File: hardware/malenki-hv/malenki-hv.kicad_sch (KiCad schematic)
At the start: 18 parts, among them J1 Conn_01x02_Male-Connector, J2 Conn_01x08_Male, J3 Conn_01x02, U2 AP2204RA-3.3TRG1, U3 ATTiny1616-MNR

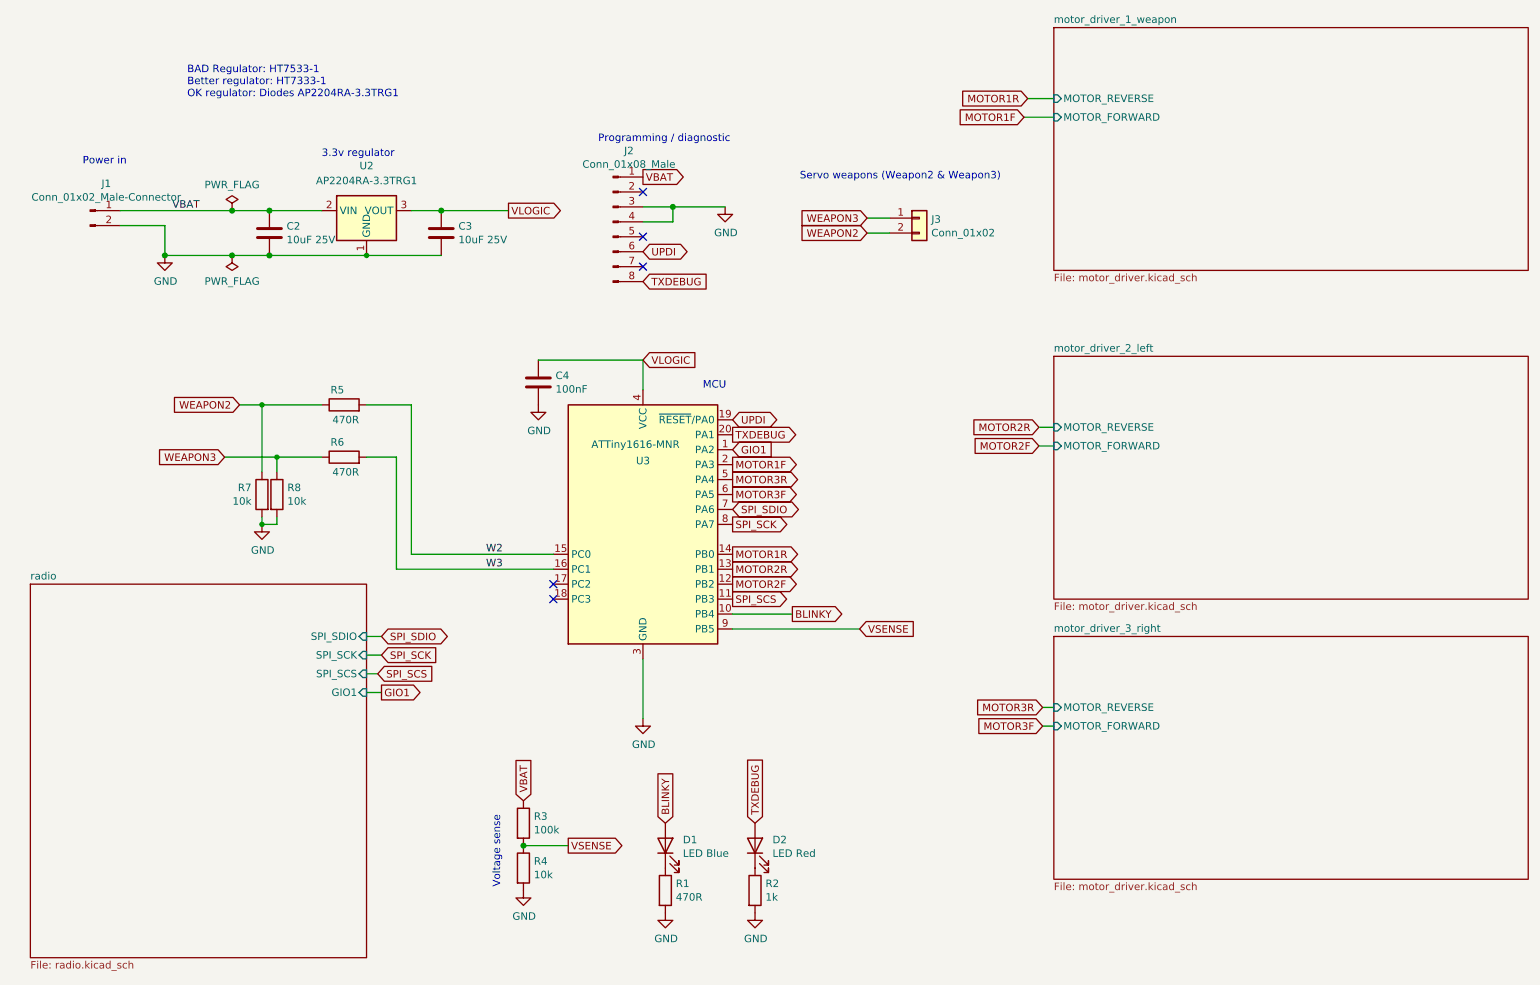
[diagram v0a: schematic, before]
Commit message: Updated u1 QFN symbol by adding solder paste layer, minor schematic updates to fix check errors, converted to kiCad 9, Updated BOM with LSCS numbers, fixed BOM errors.
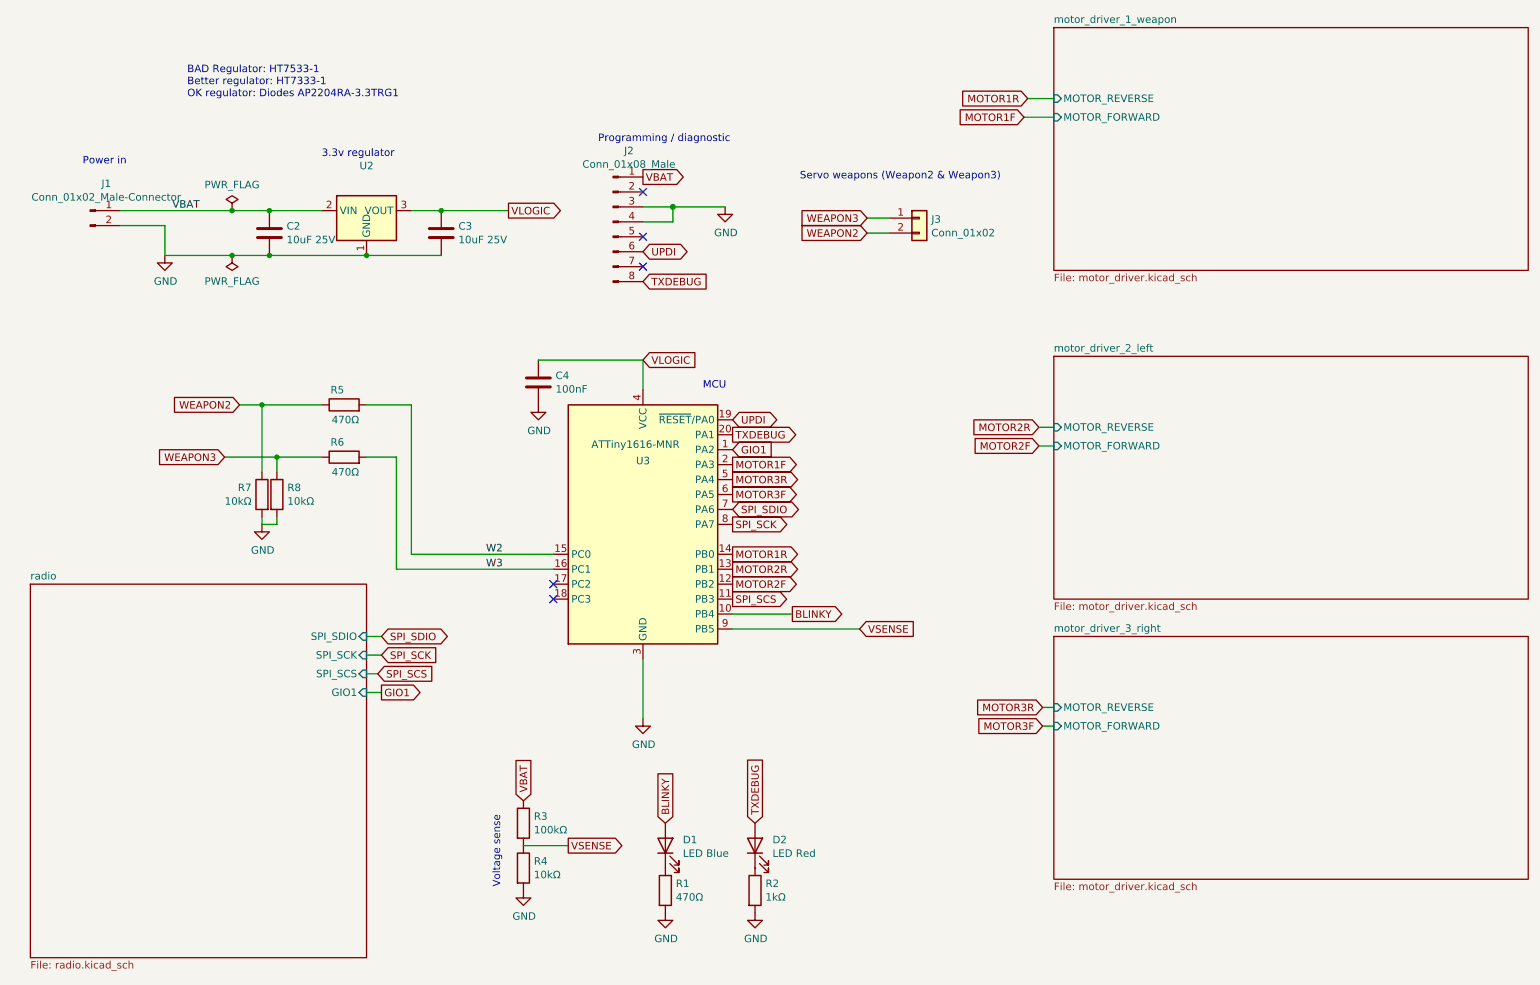
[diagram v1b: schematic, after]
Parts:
- C2, C3: MPN (none) -> CL10A106MA8NRNC
- C4: footprint Capacitor_SMD:C_0402_1005Metric_Pad0.74x0.62mm_HandSolder -> Capacitor_SMD:C_0402_1005Metric; Alternate LCSC PN (none) -> C14663; MPN (none) -> CL05B104KB54PNC; Partnum C14663 -> (none)
- D1: Alternate LCSC PN (none) -> C2689219
- R1: value 470R -> 470Ω; MPN (none) -> 0402WGF4700TCE
- R2: value 1k -> 1kΩ; MPN (none) -> 0402WGF1001TCE
- R3: value 100k -> 100kΩ; MPN (none) -> 0402WGF1003TCE; Manufacturer (none) -> Uniroyal
- R4, R7, R8: value 10k -> 10kΩ; MPN (none) -> 0402WGF1002TCE; Partnum C25804 -> (none)
- R5, R6: value 470R -> 470Ω; MPN (none) -> 0402WGF4700TCE; Manufacturer (none) -> Uniroyal
- U2: value AP2204RA-3.3TRG1 -> 300mA Fixed 3.3V Positive 24V SOT-89 Voltage Regulators - Linear, Low Drop Out (LDO) Regulators; Alternate LCSC PN (none) -> C151625; LCSC C151625 -> C7434186; MPN (none) -> HT7333-1-MS; Manufacturer Diodes -> MSKSEMI
- U3: MPN ATtiny1616-MNR -> ATTINY1616-MNR
